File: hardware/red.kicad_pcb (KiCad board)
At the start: 6 copper layers, 40 x 40 mm, 193 parts, among them J1 MICROSDCARD, J2 USB-A, J3 MICRO_HDMI, J4 USB-MINI-B-SMD, J5 STACK-UP-LOW, J6 STACK-DOWN, J7 STACK-UP-LOW, J8 STACK-DOWN, P1 Camera/EXT, Q1 2N7002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

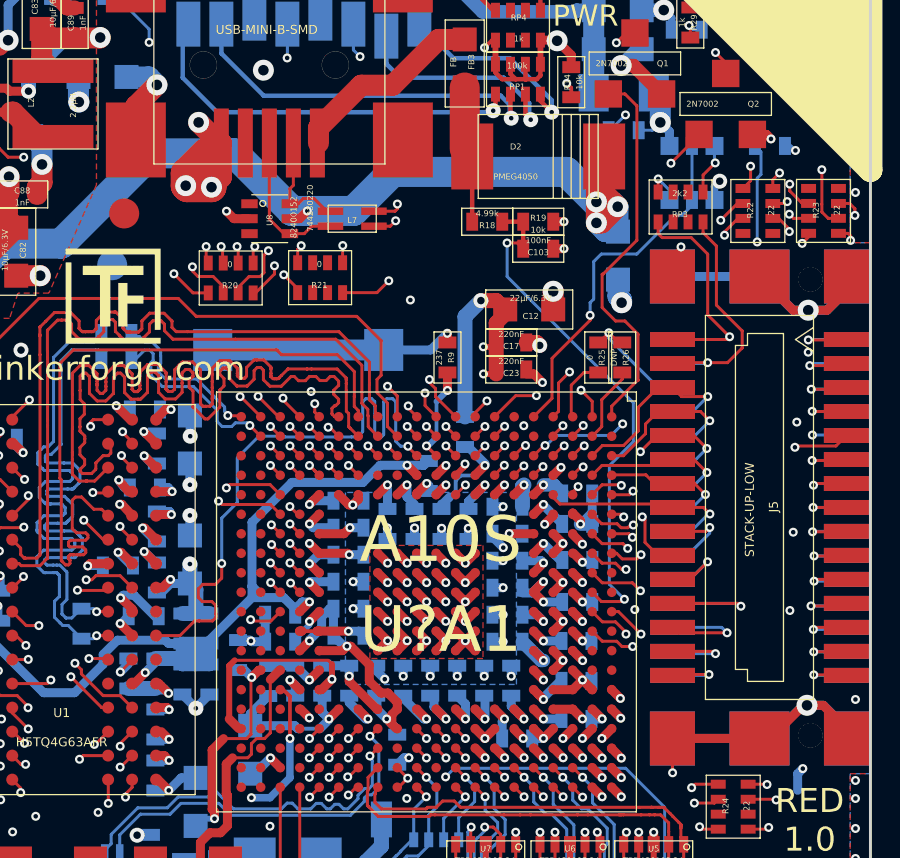
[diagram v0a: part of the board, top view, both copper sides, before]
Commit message: fix GPIO G2 input bug
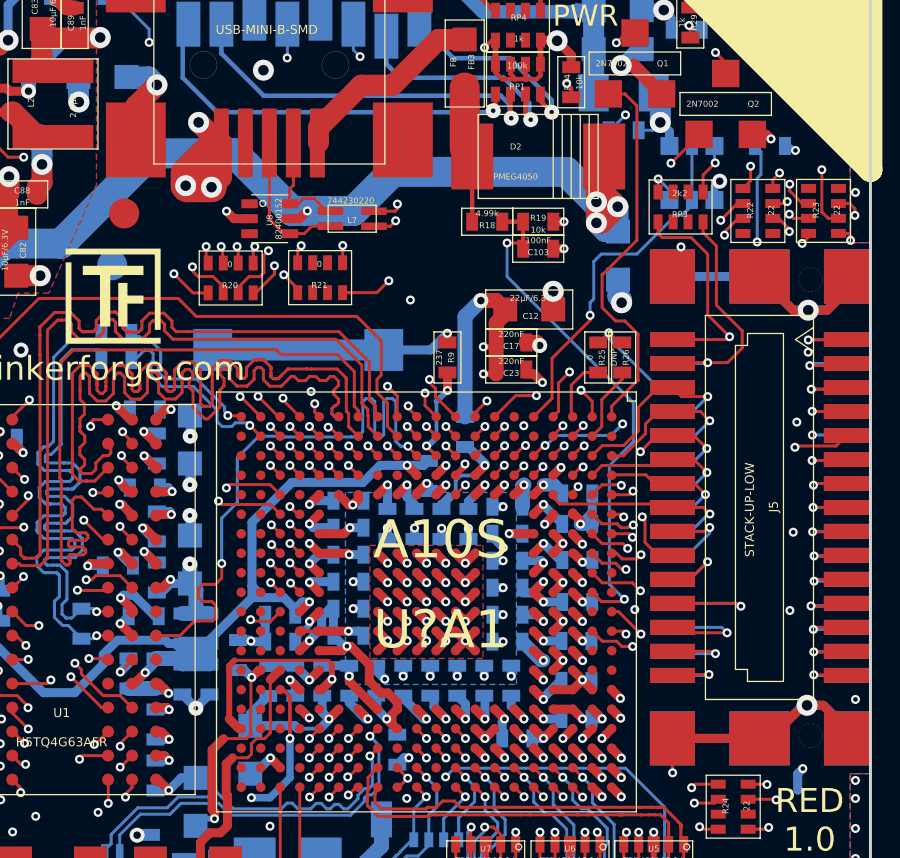
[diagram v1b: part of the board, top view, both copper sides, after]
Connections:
- U?A1 pad A12: (no net) -> STACK-EX-1-GP00
- U?A1 pad B11: STACK-EX-1-GP00 -> (no net)
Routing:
- net STACK-EX-1-GP00: track 10.4 -> 9.55 mm

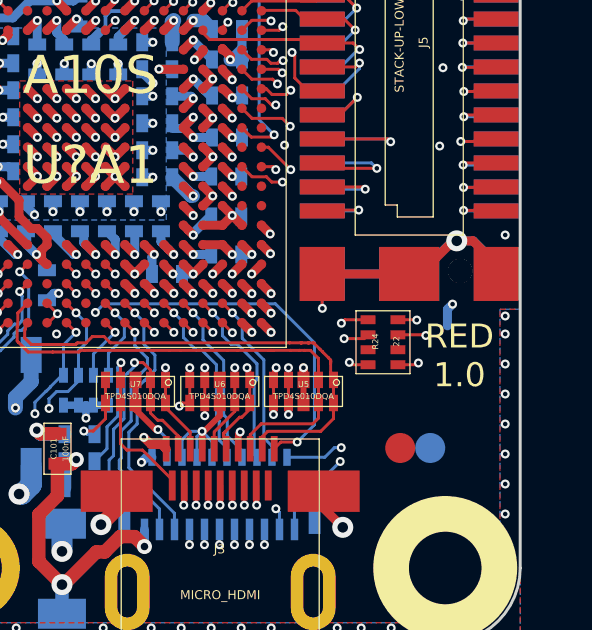
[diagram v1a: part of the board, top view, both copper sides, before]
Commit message: delete useless trace orderable version
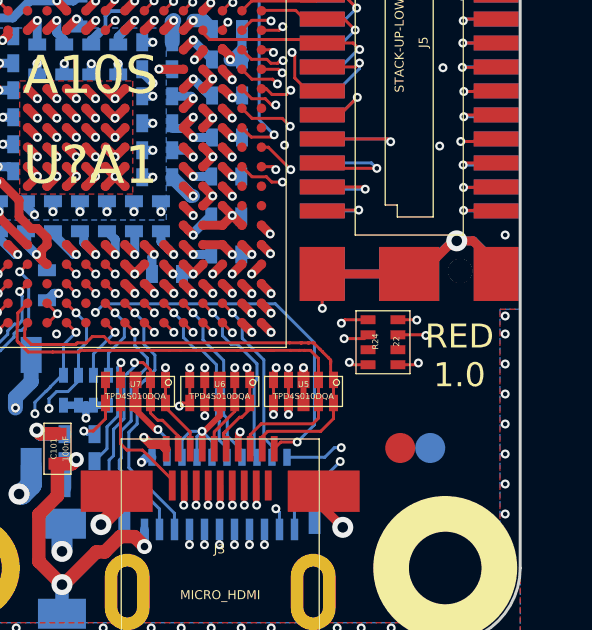
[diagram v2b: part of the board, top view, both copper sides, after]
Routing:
- net GND: track 816.8 -> 813.7 mm, vias 313 -> 312

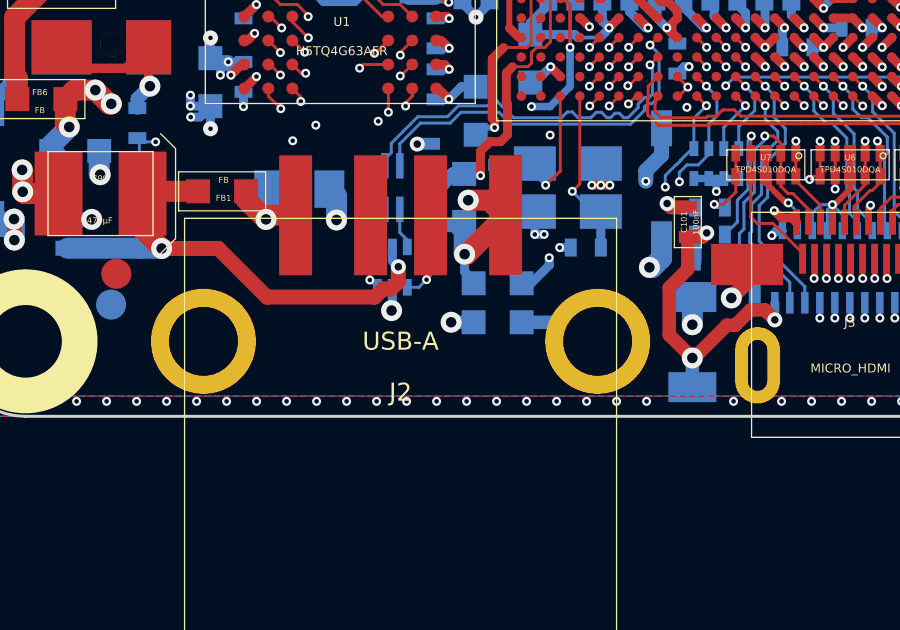
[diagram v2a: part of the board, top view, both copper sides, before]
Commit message: change footprint of usb host connector to one with pegs
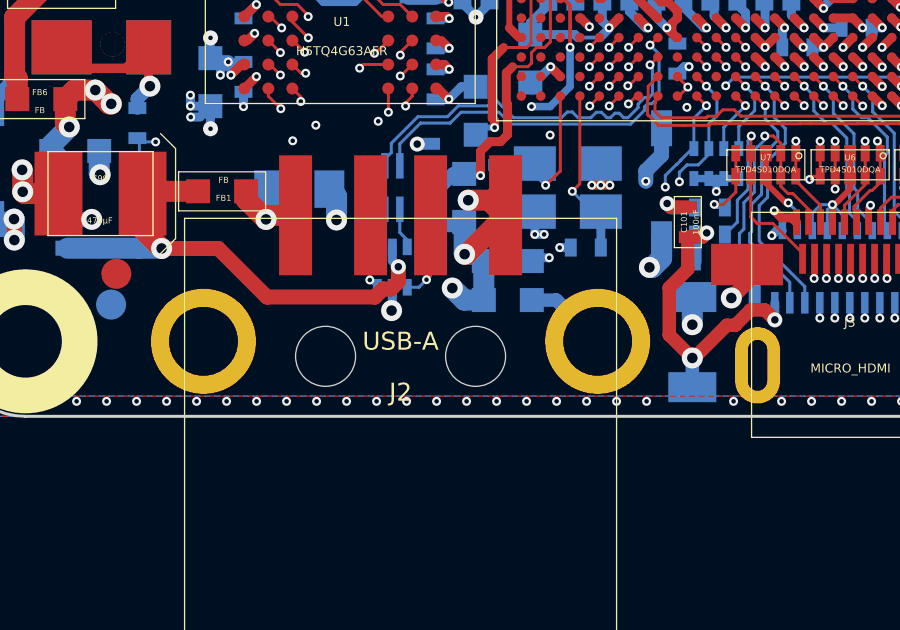
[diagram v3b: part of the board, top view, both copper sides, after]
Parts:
- J2: footprint tinkerforge:USB-A-SMT-8231 -> kicad-libraries:USB-A-SMT-8231-PEG
- moved FB2 0.81 mm to (145.9, 111.0)
- moved C25 0.81 mm to (145.9, 109.8)
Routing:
- net +5V: track 119.5 -> 121.0 mm
- net USB-HOST-DRV: track 42.2 -> 41.1 mm
- net Net-(FB2-Pad2): track 2.80 -> 3.66 mm
- net Net-(C25-Pad2): track 12.2 -> 11.4 mm
- net +3.3V: track 192.1 -> 191.6 mm
